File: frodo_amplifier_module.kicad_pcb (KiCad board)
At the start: 2 copper layers, 16.5 x 21.2 mm, 23 parts, among them IC1 INA826AID, IC2 AS321KTR-G1, J1 Conn_01x01_Socket, J2 Conn_01x01_Socket, J3 Conn_01x01_Socket, J4 Conn_01x01_Socket, J5 Conn_01x01_Socket, J6 Conn_01x01_Socket, J7 Conn_01x01_Socket, J8 Conn_01x01_Socket

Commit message: finished the scematics
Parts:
- removed IC2: AS321KTR-G1, Package_TO_SOT_SMD:SOT-23-5
- removed J5, J6, J7, J8: Conn_01x01_Socket, Connector_Wire:SolderWirePad_1x01_SMD_1x2mm
- removed REF** (x2): MountingHole_2.2mm_M2, MountingHole:MountingHole_2.2mm_M2
- removed mouse-bite-2mm-slot (x2): VAL**, MountingEquipment:mouse-bite-2mm-slot
- added C10: 2n2, Capacitor_SMD:C_0402_1005Metric, F.Cu at (80.6, 55.3)
- added C11: 470n, Capacitor_SMD:C_0402_1005Metric, F.Cu at (77.7, 59.5)
- added C12: 0u1, Capacitor_SMD:C_0402_1005Metric, F.Cu at (77.6, 63.9)
- added C13: 0u1, Capacitor_SMD:C_0402_1005Metric, F.Cu at (44.2, 80.0)
- added C14: 0u1, Capacitor_SMD:C_0402_1005Metric, F.Cu at (44.2, 81.9)
- added C15: 1u, Capacitor_SMD:C_0402_1005Metric, F.Cu at (44.2, 83.9)
- added C16: 1u, Capacitor_SMD:C_0402_1005Metric, F.Cu at (44.2, 85.9)
- added C3: 4u7, Capacitor_SMD:C_0402_1005Metric, F.Cu at (68.5, 68.7)
- added C4: 0u1, Capacitor_SMD:C_0402_1005Metric, F.Cu at (73.5, 51.4)
- added C5: 10n, Capacitor_SMD:C_0402_1005Metric, F.Cu at (71.6, 55.5)
- added C6: 2n2, Capacitor_SMD:C_0402_1005Metric, F.Cu at (73.8, 59.4)
- added C7: 10n, Capacitor_SMD:C_0402_1005Metric, F.Cu at (74.3, 64.0)
- added C8: 10n, Capacitor_SMD:C_0402_1005Metric, F.Cu at (79.9, 48.8)
- added C9: 2n2, Capacitor_SMD:C_0402_1005Metric, F.Cu at (81.2, 51.9)
- added FB2: 120R, Inductor_SMD:L_0402_1005Metric, F.Cu at (70.2, 73.8)
- added JP2: SolderJumper_3_Open, Jumper:SolderJumper-3_P1.3mm_Open_RoundedPad1.0x1.5mm, F.Cu at (103.7, 58.4)
- added JP3: SolderJumper_3_Open, Jumper:SolderJumper-3_P1.3mm_Open_RoundedPad1.0x1.5mm, F.Cu at (50.8, 76.3)
- added JP4: SolderJumper_3_Open, Jumper:SolderJumper-3_P1.3mm_Open_RoundedPad1.0x1.5mm_NumberLabels, F.Cu at (59.7, 93.9)
- added R5: 10k, Resistor_SMD:R_0402_1005Metric_Pad0.72x0.64mm_HandSolder, F.Cu at (85.7, 68.3)
- added R6: 10k, Resistor_SMD:R_0402_1005Metric_Pad0.72x0.64mm_HandSolder, F.Cu at (83.0, 72.5)
- added U1: ADC101C021CIMM, Package_SO:SSOP-8_2.95x2.8mm_P0.65mm, F.Cu at (48.0, 54.0)
- added U2: MCP6001-OT, Package_TO_SOT_SMD:SOT-23-5, F.Cu at (82.8, 79.0)
- added U3: MIC5504-3.3YM5, Package_TO_SOT_SMD:SOT-23-5, F.Cu at (45.4, 76.8)
- added U4: REF3033, Package_TO_SOT_SMD:SOT-23, F.Cu at (48.1, 81.2)
- C1: value 100n -> 10u; footprint Capacitor_SMD:C_0402_1005Metric_Pad0.74x0.62mm_HandSolder -> Capacitor_SMD:C_0402_1005Metric
- C2: value 10u -> 100n; footprint Capacitor_SMD:C_0603_1608Metric -> Capacitor_SMD:C_0402_1005Metric
- FB1: footprint Inductor_SMD:L_0603_1608Metric -> Inductor_SMD:L_0402_1005Metric
- IC1: footprint Package_SO:SOIC-8_3.9x4.9mm_P1.27mm -> Package_SON:WSON-8-1EP_3x3mm_P0.5mm_EP1.2x2mm
- J1, J2, J3, J4: value Conn_01x01_Socket -> JST-GH; footprint Connector_Wire:SolderWirePad_1x01_SMD_1x2mm -> Connector_JST:JST_GH_BM04B-GHS-TBT_1x04-1MP_P1.25mm_Vertical; moved to F.Cu
- JP1: footprint Jumper:SolderJumper-3_P1.3mm_Open_RoundedPad1.0x1.5mm_NumberLabels -> Jumper:SolderJumper-3_P1.3mm_Open_RoundedPad1.0x1.5mm; moved to F.Cu
- R1: footprint Resistor_SMD:R_0402_1005Metric_Pad0.72x0.64mm_HandSolder -> Resistor_SMD:R_0402_1005Metric
- R3: value 10k -> 5k
- RG1: footprint Resistor_SMD:R_0603_1608Metric_Pad0.98x0.95mm_HandSolder -> Resistor_SMD:R_0603_1608Metric
- moved J2 43.2 mm to (47.2, 35.2), turned to 0 degrees
- moved R3 33.4 mm to (58.5, 66.7), turned to 0 degrees
- moved IC1 27.6 mm to (95.3, 73.9)
- moved FB1 27.3 mm to (74.8, 73.5), turned to 0 degrees
- moved J4 26.8 mm to (72.0, 33.0), turned to 0 degrees
- moved J1 24.7 mm to (63.4, 43.5), turned to 0 degrees
- moved C1 21.1 mm to (67.5, 64.1), turned to 0 degrees
- moved J3 18.5 mm to (86.0, 33.9), turned to 0 degrees
- moved R1 16.3 mm to (83.9, 61.8), turned to 0 degrees
- moved R2 15.7 mm to (60.4, 60.8), turned to 0 degrees
- moved C2 14.2 mm to (67.3, 49.6), turned to 0 degrees
- moved RG1 11.6 mm to (64.4, 57.1), turned to 0 degrees
- moved R4 9.91 mm to (88.0, 64.2), turned to 0 degrees
- moved JP1 9.82 mm to (91.7, 46.5), turned to 0 degrees
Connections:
- C1 pad 1: VDD -> 5V
- C2 pad 1: VDD -> 3V3
- FB1 pad 1: Net-(J1-Pin_1) -> Net-(J1-Pin_4)
- FB1 pad 2: VDD -> 5V
- IC1 pad 7: out -> sig
- IC1 pad 8: VDD -> 3V3
- J2 pad 1: out -> Net-(J1-Pin_1)
- J3 pad 1: ref -> GND
- JP1 pad 1: GND -> sig2
- JP1 pad 2: ref -> Net-(JP1-C)
- JP1 pad 3: Net-(IC2-INPUT_-) -> sig
- R3 pad 1: Net-(IC2-INPUT_+) -> sig2
- R3 pad 2: VDD -> Net-(J3-Pin_3)
- R4 pad 2: Net-(IC2-INPUT_+) -> sig2
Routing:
- net VDD: track 31.0 -> 0.00 mm, vias 1 -> 0
- net GND: track 11.4 -> 0.00 mm, vias 17 -> 0
- net +IN: track 10.8 -> 0.00 mm, vias 1 -> 0
- net -IN: track 10.2 -> 0.00 mm, vias 1 -> 0
- net ref: track 8.19 -> 0.00 mm, vias 1 -> 0
- net out: track 6.38 -> 0.00 mm, vias 1 -> 0
- net Net-(IC2-INPUT_-): track 4.99 -> 0.00 mm, vias 1 -> 0
- net Net-(IC2-INPUT_+): track 3.28 -> 0.00 mm
- net Net-(J1-Pin_1): track 2.82 -> 0.00 mm, vias 1 -> 0
- net Net-(IC1-RG_2): track 2.44 -> 0.00 mm
- net Net-(IC1-RG_1): track 2.44 -> 0.00 mm
- removed copper zone on B.Cu, net GND
- removed copper zone on F.Cu, net GND
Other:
- board outline removed
- copper layers 2 -> 4
- board text removed: "1 gnd"
- board text removed: "3 ref"
- board text removed: "<io sens>"
- board text removed: "JLCJLCJLCJLC"
- board text removed: "o+"
- board text removed: "ref"
- board text removed: "s+"
- board text removed: "s-"
- board text removed: "u+"
- board text removed: "u-"

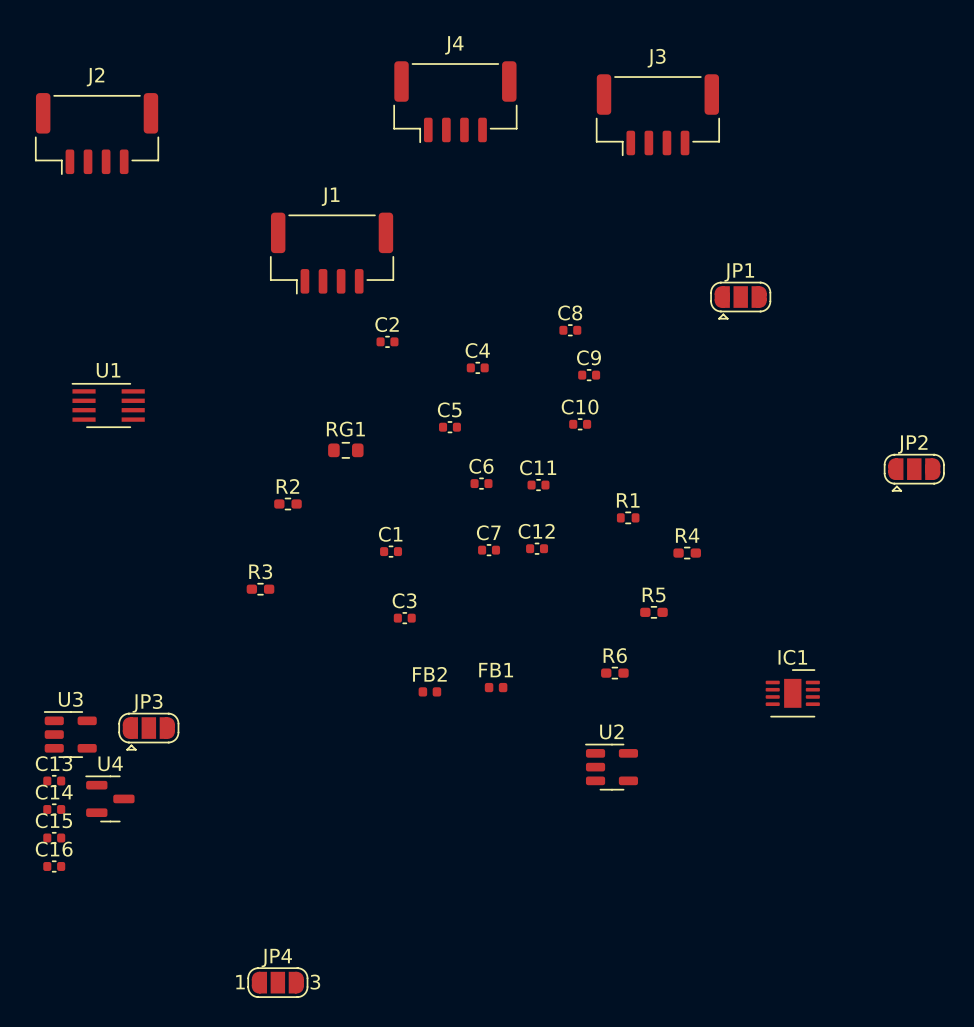
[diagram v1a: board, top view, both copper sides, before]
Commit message: started the pcb layout for the amp module
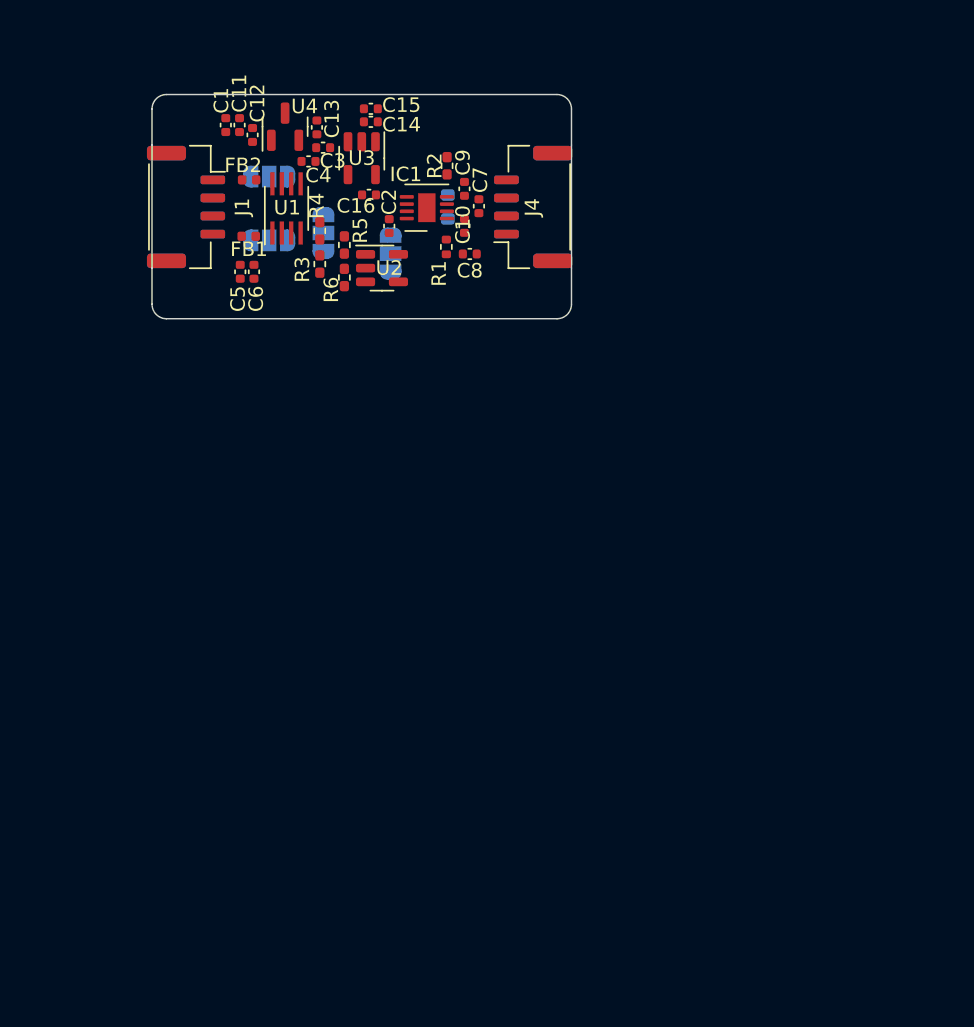
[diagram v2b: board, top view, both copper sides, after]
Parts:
- J1, J4: footprint Connector_JST:JST_GH_BM04B-GHS-TBT_1x04-1MP_P1.25mm_Vertical -> Connector_JST:JST_GH_SM04B-GHS-TB_1x04-1MP_P1.25mm_Horizontal
- J2, J3: footprint Connector_JST:JST_GH_BM04B-GHS-TBT_1x04-1MP_P1.25mm_Vertical -> Connector_JST:JST_GH_SM04B-GHS-TB_1x04-1MP_P1.25mm_Horizontal; moved to B.Cu
- JP1, JP2, JP3, JP4, RG1: moved to B.Cu
- moved C15 55.0 mm to (66.1, 33.5), turned to 180 degrees
- moved C14 52.3 mm to (66.1, 34.4), turned to 180 degrees
- moved C16 51.3 mm to (66.0, 39.4), turned to 180 degrees
- moved JP4 51.0 mm to (67.5, 43.5), turned to -90 degrees
- moved C13 48.7 mm to (62.4, 34.8), turned to 90 degrees
- moved U4 48.0 mm to (60.2, 34.7), turned to 90 degrees
- moved JP2 47.3 mm to (59.1, 42.6), turned to 180 degrees
- moved U3 44.6 mm to (65.5, 36.9), turned to -90 degrees
- moved IC1 42.0 mm to (70.0, 40.3), turned to 180 degrees
- moved JP3 39.0 mm to (59.1, 38.2), turned to 180 degrees
- moved U2 38.0 mm to (66.9, 44.5)
- moved FB2 37.5 mm to (57.7, 38.4)
- moved FB1 35.6 mm to (57.7, 42.3)
- moved C12 34.7 mm to (58.0, 35.3), turned to 90 degrees
- moved R4 33.8 mm to (62.6, 41.9), turned to -90 degrees
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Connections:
- J1 pad 2: SDA -> SCL
- J1 pad 3: SCL -> SDA
- J2 pad 2: SDA -> SCL
- J2 pad 3: SCL -> SDA
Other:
- board outline added: 29 x 15.5 mm

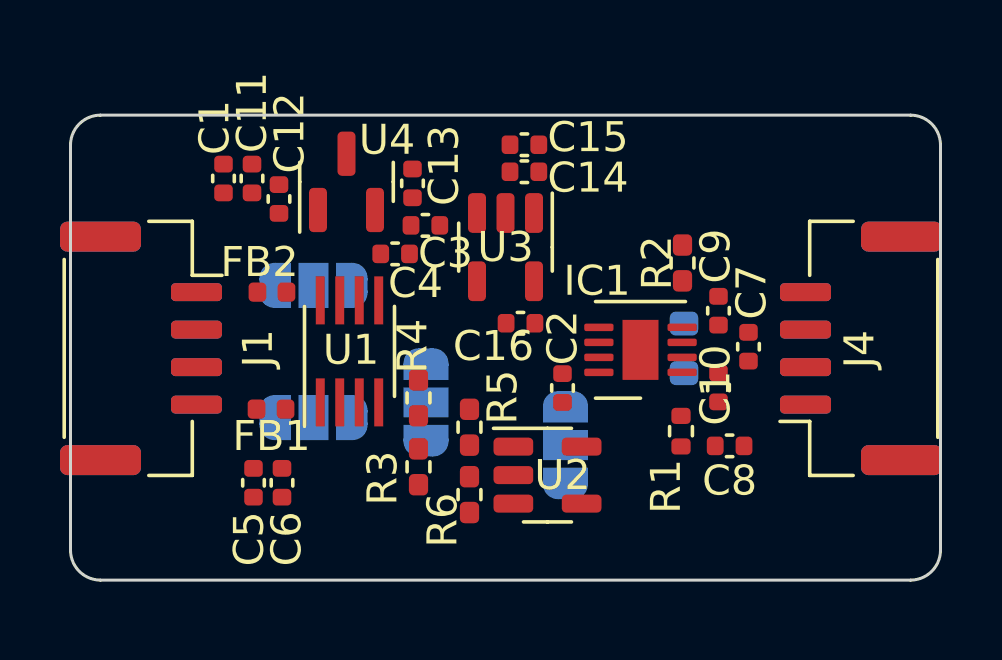
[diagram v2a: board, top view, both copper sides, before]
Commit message: finished pcb layout - routing not done yet
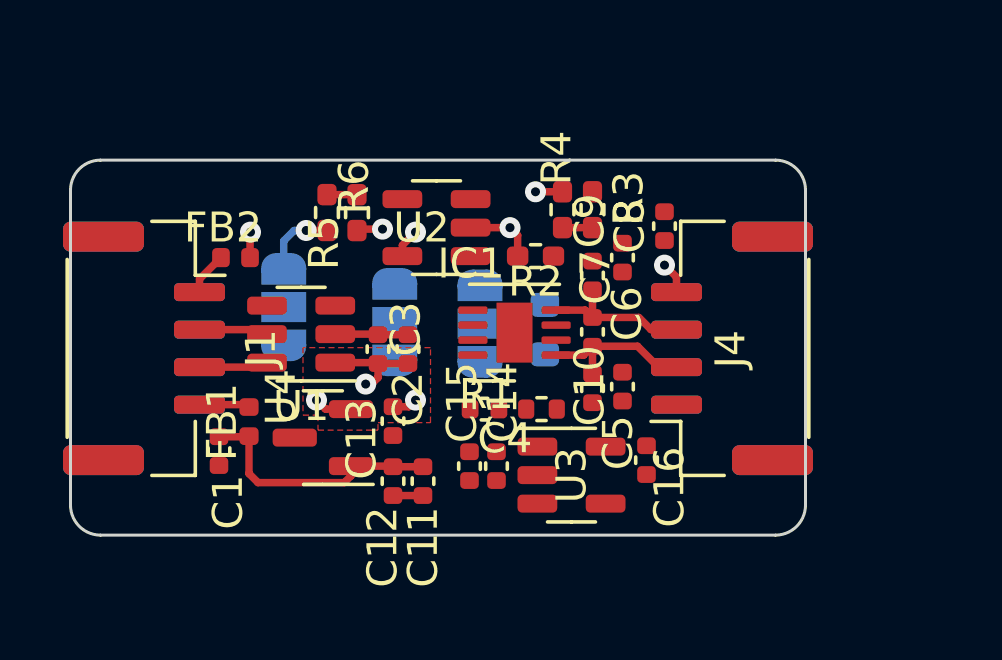
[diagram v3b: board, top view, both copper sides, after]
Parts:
- removed JP4: SolderJumper_3_Open, Jumper:SolderJumper-3_P1.3mm_Open_RoundedPad1.0x1.5mm_NumberLabels
- C2: value 100n -> 4u7
- C3: value 4u7 -> 0u1
- C4: value 0u1 -> 100n
- JP3: footprint Jumper:SolderJumper-3_P1.3mm_Open_RoundedPad1.0x1.5mm -> Jumper:SolderJumper-3_P1.3mm_Open_RoundedPad1.0x1.5mm_NumberLabels
- U1: value ADC101C021CIMM -> ADC101C021CIMK; footprint Package_SO:SSOP-8_2.95x2.8mm_P0.65mm -> Package_TO_SOT_SMD:SOT-23-6
- moved C6 13.6 mm to (69.4, 37.2)
- moved C5 12.7 mm to (69.4, 41.5)
- moved C11 11.6 mm to (62.8, 44.7), turned to -90 degrees
- moved C15 10.9 mm to (64.3, 44.2), turned to -90 degrees
- moved R6 10.5 mm to (59.5, 35.7), turned to 90 degrees
- moved R3 10.3 mm to (68.4, 35.7), turned to 90 degrees
- moved C12 10.1 mm to (61.8, 44.7), turned to -90 degrees
- moved C14 9.86 mm to (65.2, 44.2), turned to -90 degrees
- moved C1 9.09 mm to (56.0, 43.7), turned to -90 degrees
- moved U2 9.04 mm to (63.2, 36.2), turned to 180 degrees
- moved U4 8.56 mm to (59.4, 43.2), turned to 180 degrees
- moved R5 8.08 mm to (60.5, 35.8), turned to -90 degrees
- moved C13 7.95 mm to (61.8, 42.7), turned to -90 degrees
- moved U3 7.91 mm to (67.7, 44.5), turned to 0 degrees
- moved R4 7.90 mm to (67.4, 35.7)
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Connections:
- C2 pad 1: 3V3 -> 3V3Ref
- C4 pad 1: 3V3Ref -> 3V3
- J2 pad 1: Net-(J1-Pin_1) -> Net-(J1-Pin_4)
- J2 pad 2: SCL -> SDA
- J2 pad 3: SDA -> SCL
- J2 pad 4: Net-(J1-Pin_4) -> Net-(J1-Pin_1)
- JP3 pad 2: Net-(JP3-C) -> ref
- JP3 pad 3: 3V3 -> Net-(JP3-B)
- R5 pad 2: 3V3Ref -> 3V3
- U1 pad 1: SDA -> 3V3Ref
- U1 pad 2: unconnected-(U1-ALERT-Pad2) -> GND
- U1 pad 3: Net-(JP2-C) -> Net-(JP1-C)
- U1 pad 4: Net-(JP1-C) -> Net-(JP2-C)
- U1 pad 5: 3V3Ref -> SCL
- U1 pad 6: Net-(JP3-C) -> SDA
- U2 pad 1: Net-(JP4-B) -> Net-(JP3-B)
- U2 pad 4: Net-(JP4-B) -> Net-(JP3-B)
- U2 pad 5: 3V3Ref -> 3V3
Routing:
- net GND: track 0.00 -> 10.1 mm, vias 0 -> 4
- net 5V: track 0.28 -> 8.61 mm
- net 3V3Ref: track 0.00 -> 5.52 mm, vias 0 -> 3
- net -IN: track 0.00 -> 5.42 mm
- net +IN: track 0.00 -> 5.33 mm
- net 3V3: track 0.00 -> 2.92 mm, vias 0 -> 3
- net SDA: track 0.00 -> 2.36 mm
- net SCL: track 0.00 -> 2.36 mm
- net Net-(J1-Pin_1): track 0.00 -> 2.00 mm
- net Net-(J1-Pin_4): track 0.00 -> 1.68 mm
- net Net-(U2-+): track 0.00 -> 1.00 mm
- net sig2: track 0.00 -> 1.00 mm
- added copper zone on In2.Cu, net 3V3
- added copper zone on F.Cu, net 3V3Ref
- added copper zone on In2.Cu, net 3V3Ref
- added copper zone on In1.Cu, net GND
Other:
- board size 29 x 15.5 mm -> 24.5 x 12.5 mm

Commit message: finished routing -> pcb should be ready to order after review
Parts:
- moved C7 0.95 mm to (69.3, 39.7)
- moved C5 0.56 mm to (69.2, 42.0), turned to 90 degrees
- moved R2 0.40 mm to (66.7, 37.5)
- moved C4 0.36 mm to (64.7, 42.6)
- moved R1 0.35 mm to (66.7, 42.0)
- moved JP2 0.31 mm to (57.8, 38.9)
- moved C9 0.20 mm to (68.4, 38.0)
- moved JP1 0.16 mm to (61.6, 39.4)
- moved FB1 0.15 mm to (57.1, 42.7)
- moved JP3 0.15 mm to (64.8, 39.5)
- moved C10 0.12 mm to (68.3, 41.5)
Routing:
- net GND: track 10.1 -> 38.6 mm, vias 4 -> 17
- net 5V: track 8.61 -> 22.5 mm, vias 0 -> 2
- net 3V3: track 2.92 -> 15.3 mm, vias 3 -> 5
- net Net-(J3-Pin_3): track 0.00 -> 9.86 mm, vias 0 -> 1
- net Net-(U2-+): track 1.00 -> 9.88 mm, vias 0 -> 2
- net sig2: track 1.00 -> 7.52 mm, vias 0 -> 1
- net Net-(JP1-C): track 0.00 -> 4.94 mm, vias 0 -> 1
- net Net-(JP3-B): track 0.00 -> 4.86 mm, vias 0 -> 1
- net sig: track 0.00 -> 3.94 mm, vias 0 -> 1
- net Net-(IC1-RG_1): track 0.00 -> 3.08 mm, vias 0 -> 1
- net ref: track 0.00 -> 2.93 mm, vias 0 -> 1
- net Net-(IC1-RG_2): track 0.00 -> 2.72 mm, vias 0 -> 1
- net Net-(JP2-C): track 0.00 -> 2.04 mm, vias 0 -> 1
- net Net-(J1-Pin_4): track 1.68 -> 3.08 mm, vias 0 -> 1
- net +IN: track 5.33 -> 6.58 mm
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- added copper zone on F.Cu, net GND

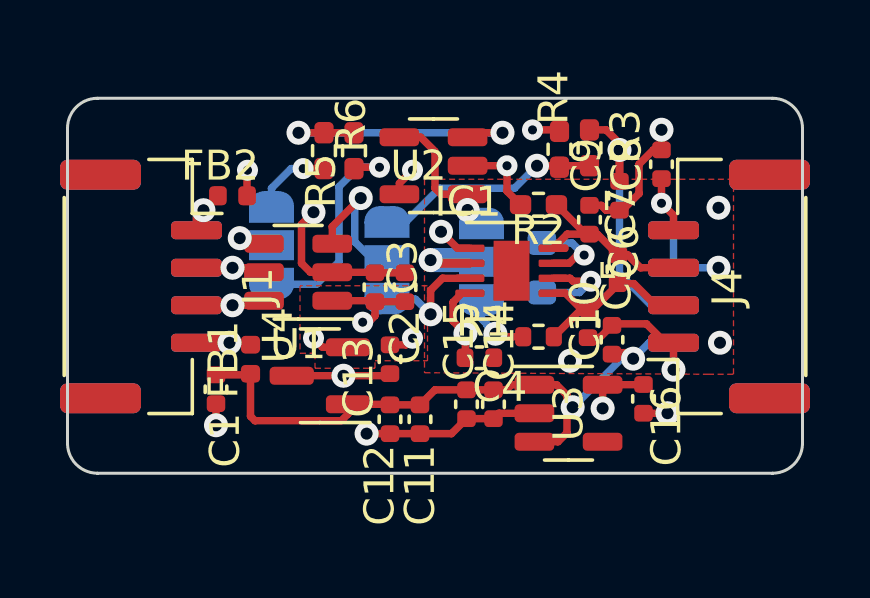
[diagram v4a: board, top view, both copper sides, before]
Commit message: optimised via placement
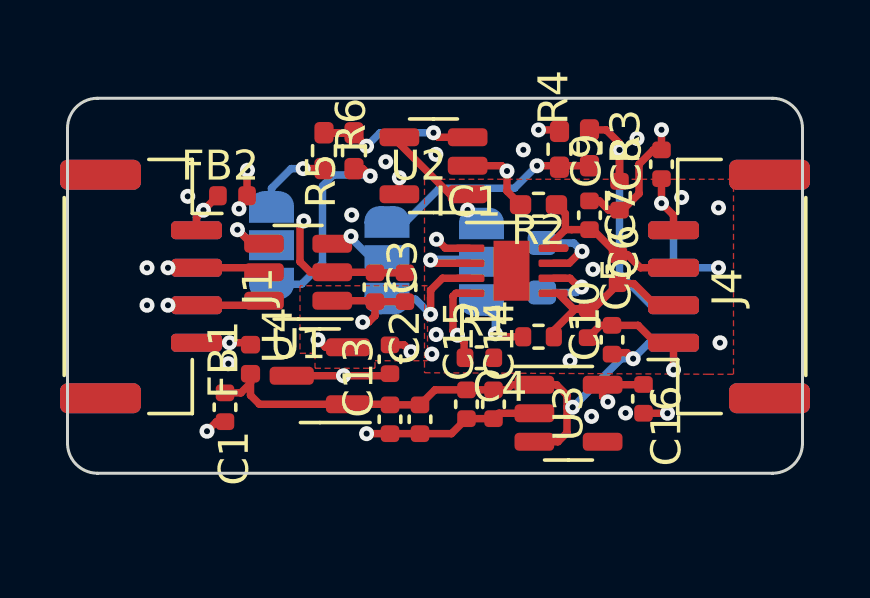
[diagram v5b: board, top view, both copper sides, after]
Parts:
- moved C1 0.67 mm to (56.2, 44.3)
- moved C9 0.15 mm to (68.4, 37.9)
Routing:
- net Net-(U2-+): track 9.88 -> 6.22 mm
- net Net-(JP1-C): track 4.94 -> 2.45 mm
- net 5V: track 22.5 -> 20.8 mm
- net 3V3: track 15.3 -> 14.3 mm
- net SDA: track 3.56 -> 4.21 mm
- net SCL: track 3.56 -> 4.21 mm
- net GND: track 38.6 -> 37.9 mm, vias 17 -> 33
- net Net-(IC1-RG_1): track 3.08 -> 2.47 mm
- net Net-(JP3-B): track 4.86 -> 4.27 mm

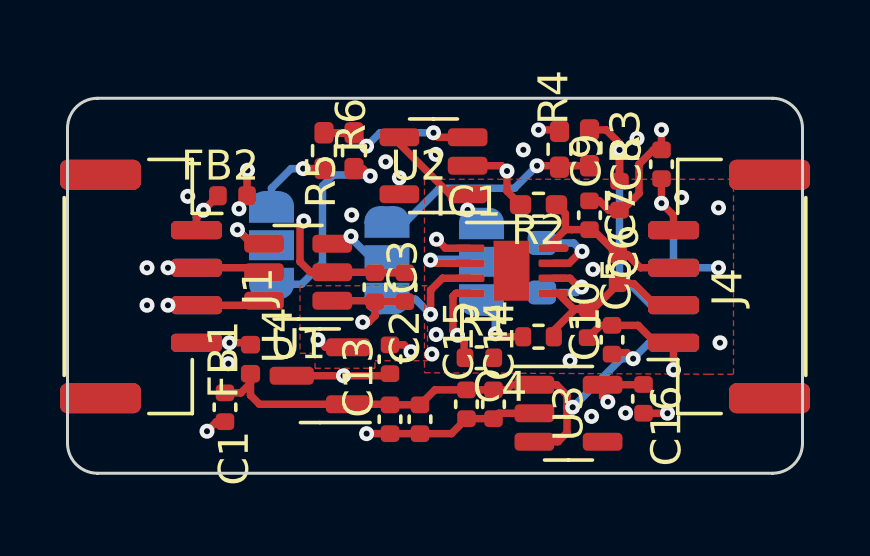
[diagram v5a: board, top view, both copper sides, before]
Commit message: fixed silkscreen
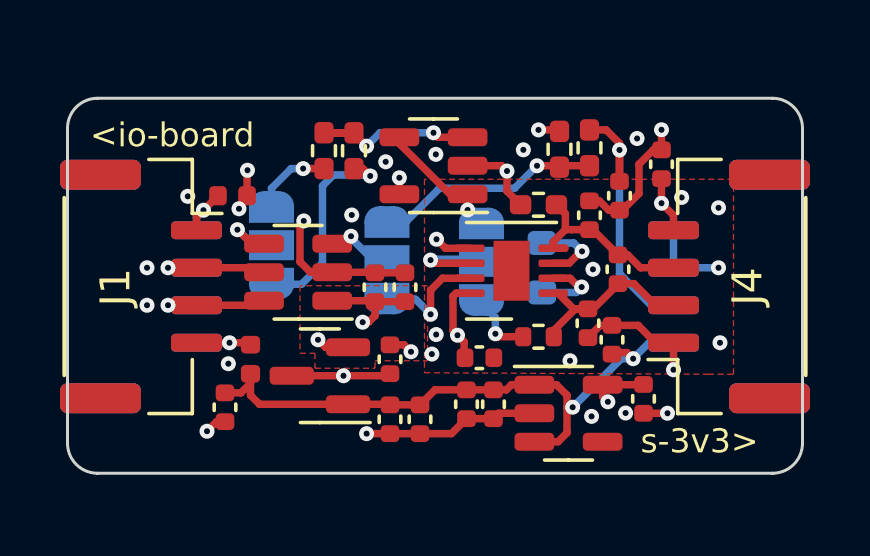
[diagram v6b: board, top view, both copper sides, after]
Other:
- board text added: "<io-board"
- board text added: "<s-5v"
- board text added: "next amp>"
- board text added: "s-3v3>"
